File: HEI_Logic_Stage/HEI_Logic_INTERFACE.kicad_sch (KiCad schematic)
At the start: 101 parts, among them J1 Conn_02x07_Odd_Even, J2 Conn_02x07_Odd_Even, J4 430451210, U1 CD40109BQNSRQ1, U16 TLV9051IDBVR, U3 TLV9051IDBVR, U4 TLV9051IDBVR, U7 TLV9051IDBVR, U8 TLV9051IDBVR

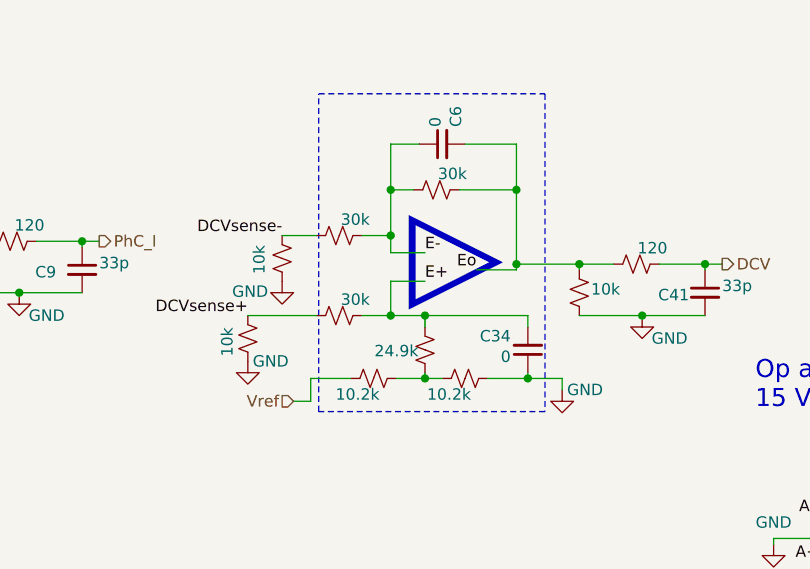
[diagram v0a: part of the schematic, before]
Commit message: updated resistor mappings for logic amps
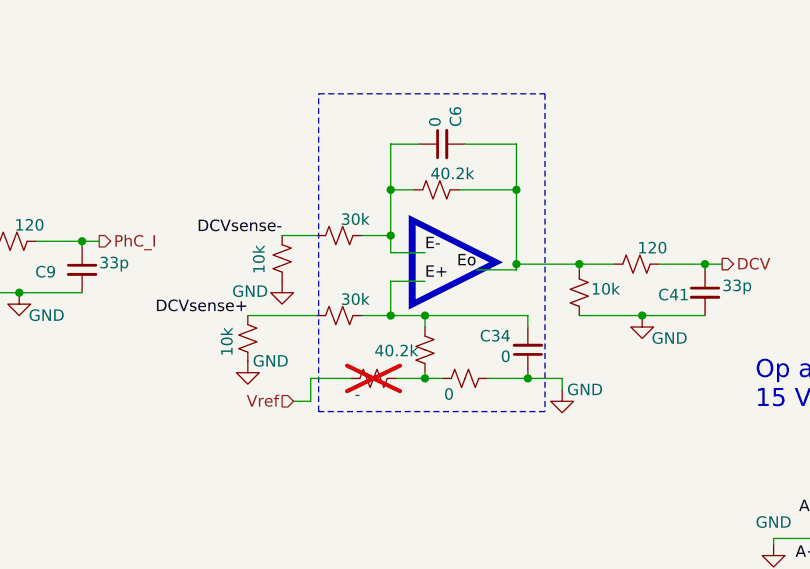
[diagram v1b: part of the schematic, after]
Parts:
- R65: value 10.2k -> -; now not fitted
- R71: value 24.9k -> 40.2k
- R72: value 30k -> 40.2k
- R77: value 10.2k -> 0
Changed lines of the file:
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@@
 			)
 		)
-		(property "Value" "30k"
+		(property "Value" "40.2k"
 			(at 228.473 110.617 90)
 			(effects
@@
 			)
 		)
-		(property "Value" "24.9k"
+		(property "Value" "40.2k"
 			(at 222.25 130.302 0)
 			(effects
@@
 		(in_bom yes)
 		(on_board yes)
-		(dnp no)
+		(dnp yes)
 		(property "Reference" "R65"
 			(at 219.71 135.255 90)
@@
 			)
 		)
-		(property "Value" "10.2k"
+		(property "Value" "-"
 			(at 217.932 135.128 90)
 			(effects
@@
 			)
 		)
-		(property "Value" "10.2k"
+		(property "Value" "0"
 			(at 228.092 135.128 90)
 			(effects

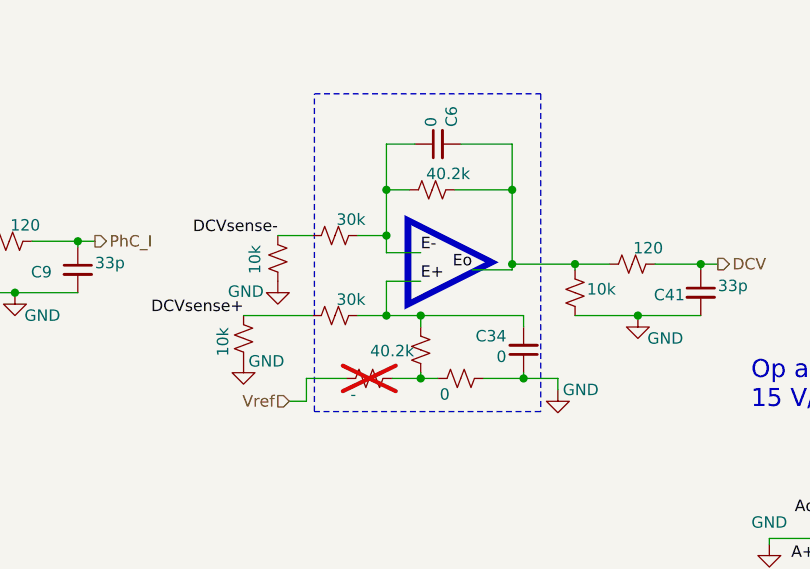
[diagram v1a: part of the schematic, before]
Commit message: final dcv amp resistor vals
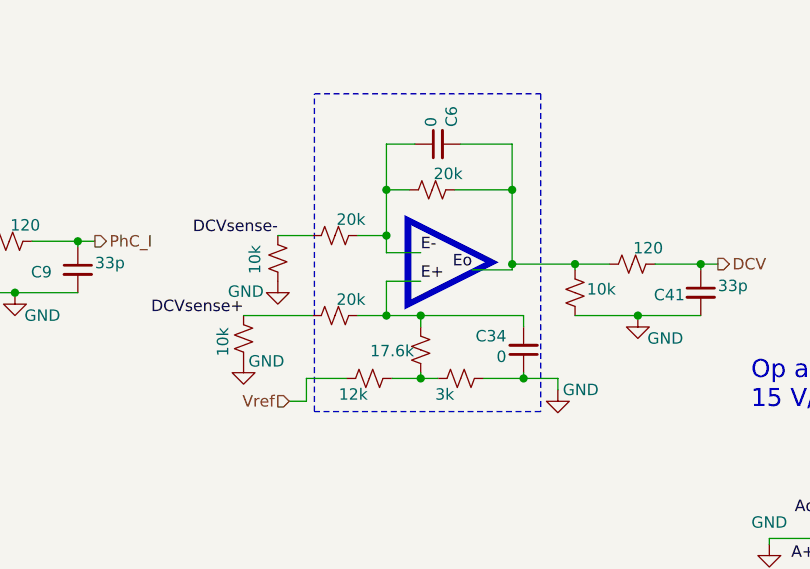
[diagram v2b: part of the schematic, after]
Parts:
- R63, R64: value 30k -> 20k
- R65: value - -> 12k; now fitted
- R71: value 40.2k -> 17.6k
- R72: value 40.2k -> 20k
- R77: value 0 -> 3k
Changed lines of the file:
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@@
 			)
 		)
-		(property "Value" "40.2k"
+		(property "Value" "20k"
 			(at 228.473 110.617 90)
 			(effects
@@
 			)
 		)
-		(property "Value" "40.2k"
+		(property "Value" "17.6k"
 			(at 222.25 130.302 0)
 			(effects
@@
 		(in_bom yes)
 		(on_board yes)
-		(dnp yes)
+		(dnp no)
 		(property "Reference" "R65"
 			(at 219.71 135.255 90)
@@
 			)
 		)
-		(property "Value" "-"
+		(property "Value" "12k"
 			(at 217.932 135.128 90)
 			(effects
@@
 			)
 		)
-		(property "Value" "0"
+		(property "Value" "3k"
 			(at 228.092 135.128 90)
 			(effects
@@
 			)
 		)
-		(property "Value" "30k"
+		(property "Value" "20k"
 			(at 217.678 124.587 90)
 			(effects
@@
 			)
 		)
-		(property "Value" "30k"
+		(property "Value" "20k"
 			(at 217.678 115.697 90)
 			(effects

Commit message: added horizontal b2b connector info/3d model
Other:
- note added: "Current inputs: 0.55V-4.45V, centered at 2.55V (ZCR) - diff amp with gain of 3/4 transforms to ~3Vpp centered on Vodc Vodc = 1.65V (half of 3v3) DCVsense input ranges 0-2Vpp with 1.44 Vcm. Diff amplifier with unity gain transforms to 0-2Vpp centered on Vodc. Vocm generated through resistor divider and feedback network around op amps. 3V3 divider also acts as part of lower resistor for non-inv inp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"
- note added: "Datasheet for horizontal header"
- note added: "Datasheet for vertical header"
- note added: "Use same header type for both connectors. Horizontal header allows for 90deg B2B to probe power stage more easily. Vertical header is intended for final compact design with parallel stack B2B."
- note removed: "Current inputs: 0.55V-4.45V, centered at 2.55V (ZCR) - diff amp with gain of 3/4 transforms to ~3Vpp centered on Vodc Vodc = 1.65V (half of 3v3) DCVsense input ranges 0-2Vpp with 1.44 Vcm. Diff amplifier with unity gain transforms to 0-2Vpp centered on Vodc. Vocm generated through resistor divider and feedback network around op amps. 10k divider also acts as part of lower resistor for non-inv inp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"
- moved on the sheet: C1, C11, C2, C30, C31, C32, C33, C34, C35, C36, C37, C38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
